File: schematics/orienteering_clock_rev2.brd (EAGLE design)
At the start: 100 x 81.3 mm, 66 parts, among them IC1 TPIC6B595N, IC2 TPIC6B595N, J2 ICSP, Q1 IRFU9024V, Q2 IRFU9024V, Q3 IRFU9024V, Q4 IRFU9024V, Q5 IRFU9024V, Q6 IRFU9024V, T1 BC547, Y1 16MHz

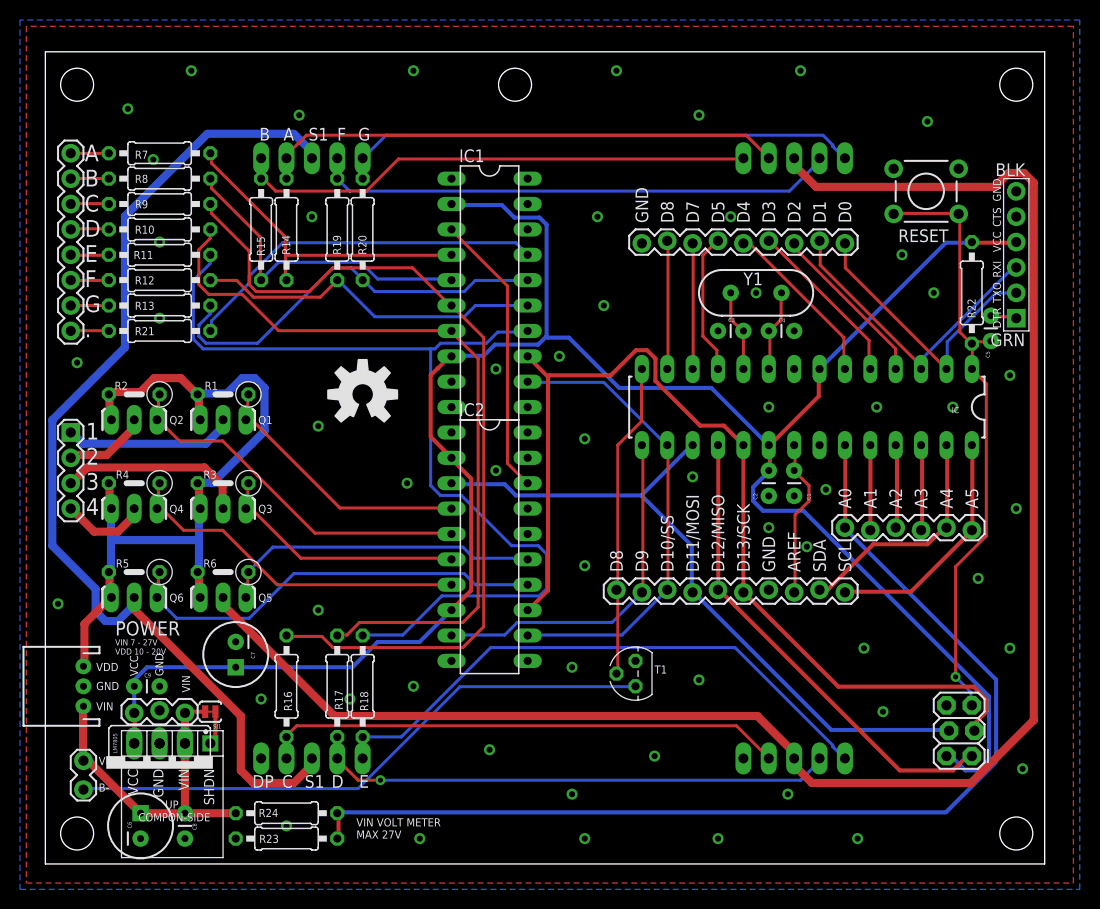
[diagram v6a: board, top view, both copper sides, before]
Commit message: schematics: improve silkscreen
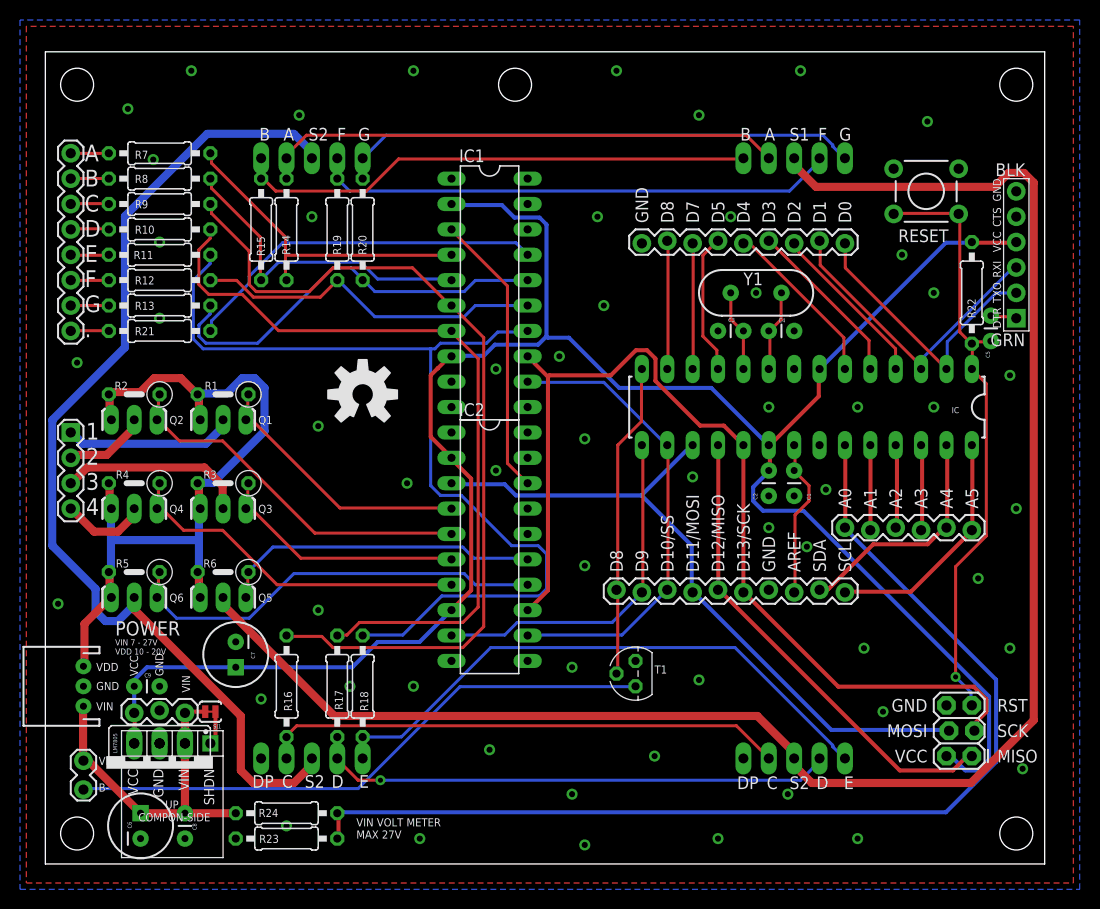
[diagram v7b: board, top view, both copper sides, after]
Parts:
- added E$2: (no value), MINE:DARWINIA-LOGO
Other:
- board text added: "For power you can either use POLOLU step-down buck converter or LM7085 with caps"
- board text added: "MISO"
- board text added: "MOSI"
- board text added: "NALAJCIE.ORG"
- board text added: "ORIENTEERING CLOCK DRIVER v2.0"
- board text added: "RST"
- board text added: "S2"
- board text added: "SCK"
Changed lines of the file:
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@@
 <text x="22.479" y="73.66" size="1.27" layer="25" font="vector" rot="R180">B</text>
 <text x="24.892" y="73.66" size="1.27" layer="25" font="vector" rot="R180">A</text>
-<text x="28.321" y="73.66" size="1.27" layer="25" font="vector" rot="R180">S1</text>
+<text x="28.321" y="73.66" size="1.27" layer="25" font="vector" rot="R180">S2</text>
 <text x="30.099" y="73.66" size="1.27" layer="25" font="vector" rot="R180">F</text>
 <text x="32.512" y="73.66" size="1.27" layer="25" font="vector" rot="R180">G</text>
 <text x="22.86" y="8.89" size="1.27" layer="25" font="vector" rot="R180">DP</text>
 <text x="24.765" y="8.89" size="1.27" layer="25" font="vector" rot="R180">C</text>
-<text x="27.94" y="8.89" size="1.27" layer="25" font="vector" rot="R180">S1</text>
+<text x="27.94" y="8.89" size="1.27" layer="25" font="vector" rot="R180">S2</text>
 <text x="29.845" y="8.89" size="1.27" layer="25" font="vector" rot="R180">D</text>
 <text x="32.385" y="8.89" size="1.27" layer="25" font="vector" rot="R180">E</text>
+<text x="25.4" y="31.115" size="1.27" layer="51" font="vector">NALAJCIE.ORG</text>
+<text x="70.612" y="73.66" size="1.27" layer="25" font="vector" rot="R180">B</text>
+<text x="73.025" y="73.66" size="1.27" layer="25" font="vector" rot="R180">A</text>
+<text x="76.454" y="73.66" size="1.27" layer="25" font="vector" rot="R180">S1</text>
+<text x="78.232" y="73.66" size="1.27" layer="25" font="vector" rot="R180">F</text>
+<text x="80.645" y="73.66" size="1.27" layer="25" font="vector" rot="R180">G</text>
+<text x="71.374" y="8.763" size="1.27" layer="25" font="vector" rot="R180">DP</text>
+<text x="73.279" y="8.763" size="1.27" layer="25" font="vector" rot="R180">C</text>
+<text x="76.454" y="8.763" size="1.27" layer="25" font="vector" rot="R180">S2</text>
+<text x="78.359" y="8.763" size="1.27" layer="25" font="vector" rot="R180">D</text>
+<text x="80.899" y="8.763" size="1.27" layer="25" font="vector" rot="R180">E</text>
+<text x="50.165" y="76.2" size="1.778" layer="51">ORIENTEERING CLOCK DRIVER v2.0</text>
+<text x="46.355" y="2.54" size="0.8128" layer="51">For power you can either use POLOLU step-down
+buck converter or LM7085 with caps</text>
+<text x="88.265" y="16.51" size="1.27" layer="25" font="vector" rot="R180">GND</text>
+<text x="88.265" y="13.97" size="1.27" layer="25" font="vector" rot="R180">MOSI</text>
+<text x="88.265" y="11.43" size="1.27" layer="25" font="vector" rot="R180">VCC</text>
+<text x="95.25" y="16.51" size="1.27" layer="25" font="vector" rot="R180" align="bottom-right">RST</text>
+<text x="95.25" y="13.97" size="1.27" layer="25" font="vector" rot="R180" align="bottom-right">SCK</text>
+<text x="95.25" y="11.43" size="1.27" layer="25" font="vector" rot="R180" align="bottom-right">MISO</text>
 </plain>
 <attributes>
@@
 <element name="IOL" library="SparkFun-Connectors" package="1X09_LOCK" value="M09LOCK" x="80.01" y="62.23" smashed="yes" rot="R180"/>
 <element name="J2" library="SparkFun-Connectors" package="2X3_LOCK" value="ICSP" x="92.71" y="10.795" smashed="yes" rot="R90">
-<attribute name="VALUE" x="95.885" y="9.525" size="1.27" layer="27" rot="R90"/>
+<attribute name="VALUE" x="93.345" y="8.89" size="1.27" layer="27" rot="R180"/>
 </element>
 <element name="JP1" library="SparkFun-Connectors" package="JST-3-PTH" value="DC_IN" x="3.81" y="17.78" smashed="yes" rot="R90">
@@
 </element>
 <element name="E$1" library="SparkFun-Aesthetics" package="OSHW-LOGO-L" value="" x="31.75" y="46.99"/>
+<element name="E$2" library="MINE" package="DARWINIA-LOGO" value="" x="31.75" y="38.735"/>
 </elements>
 <signals>
@@
 <via x="45.085" y="49.53" extent="1-16" drill="0.6096"/>
 <via x="36.83" y="17.78" extent="1-16" drill="0.6096"/>
-<via x="30.48" y="16.51" extent="1-16" drill="0.6096"/>
+<via x="30.48" y="17.78" extent="1-16" drill="0.6096"/>
 <via x="21.59" y="16.51" extent="1-16" drill="0.6096"/>
 <via x="74.295" y="6.985" extent="1-16" drill="0.6096"/>
 <via x="37.465" y="2.54" extent="1-16" drill="0.6096"/>
-<via x="53.975" y="2.54" extent="1-16" drill="0.6096"/>
+<via x="53.975" y="1.905" extent="1-16" drill="0.6096"/>
 <via x="67.31" y="2.54" extent="1-16" drill="0.6096"/>
 <via x="81.28" y="2.54" extent="1-16" drill="0.6096"/>
@@
 <via x="93.345" y="28.575" extent="1-16" drill="0.6096"/>
 <via x="97.155" y="35.56" extent="1-16" drill="0.6096"/>
-<via x="90.805" y="45.72" extent="1-16" drill="0.6096"/>
-<via x="83.185" y="45.72" extent="1-16" drill="0.6096"/>
+<via x="88.9" y="45.72" extent="1-16" drill="0.6096"/>
+<via x="81.28" y="45.72" extent="1-16" drill="0.6096"/>
 <via x="76.2" y="31.75" extent="1-16" drill="0.6096"/>
 <via x="81.915" y="21.59" extent="1-16" drill="0.6096"/>
@@
 <wire x1="17.018" y1="12.573" x2="16.51" y2="12.065" width="0.4064" layer="1"/>
 </signal>
+<signal name="A_S3" class="1">
+</signal>
+<signal name="LS_D1">
+</signal>
 </signals>

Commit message: schematics: finishing touches
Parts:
- JP1: device SparkFun-Connectors:JST-3-PTH -> SparkFun-Connectors:MOLEX-1X3
- LM7805: device v-reg:78XXS -> MINE:78XXS
- moved JP1 2.54 mm to (3.81, 15.2)
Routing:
- net A_B1: track 17.1 -> 23.8 mm
- net A_S2: track 104.3 -> 101.0 mm
- net VIN: track 45.2 -> 44.5 mm
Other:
- board text added: "ORIENTEERING CLOCK DRIVER"
- board text added: "rev 2.0"
- board text removed: "ORIENTEERING CLOCK DRIVER v2.0"
